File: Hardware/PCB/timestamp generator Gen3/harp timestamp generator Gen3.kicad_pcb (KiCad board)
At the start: 4 copper layers, 124.5 x 80.4 mm, 153 parts, among them IC1 MCP73831, IC10 SN74LVC1G125DBVT, IC11 LP5951MFX-3.3/NOPB, IC12 SI8621BC, IC13 SI8621BC, IC14 SI8621BC, IC15 SI8621BC, IC16 SI8621BC, IC17 SI8621BC, IC18 SN74LVC1G125DBVT, IC19 SN74LVC1G125DBVT, IC2 USBLC6-2SC6, IC3 FT232RL-REEL, IC4 TPS2114, IC5 LP5951MFX-3.3/NOPB, IC6 ATXMEGA16A4U-A, IC7 M74VHC1GT126DF1G, IC8 M74VHC1GT126DF1G, IC9 M74VHC1GT126DF1G, Q1 RTU002P02T106, Q2 BC817-40W, Q3 SBC817, Q4 DMG1012UW, Q5 DMP2035U-7, T1 BC850, T10 BC850, T2 BC850, T3 BC850, T4 BC850, T5 BC850, T6 BC850, T7 BC850, T8 BC850, T9 BC850, X1 B2B-XH-A(LF)(SN)

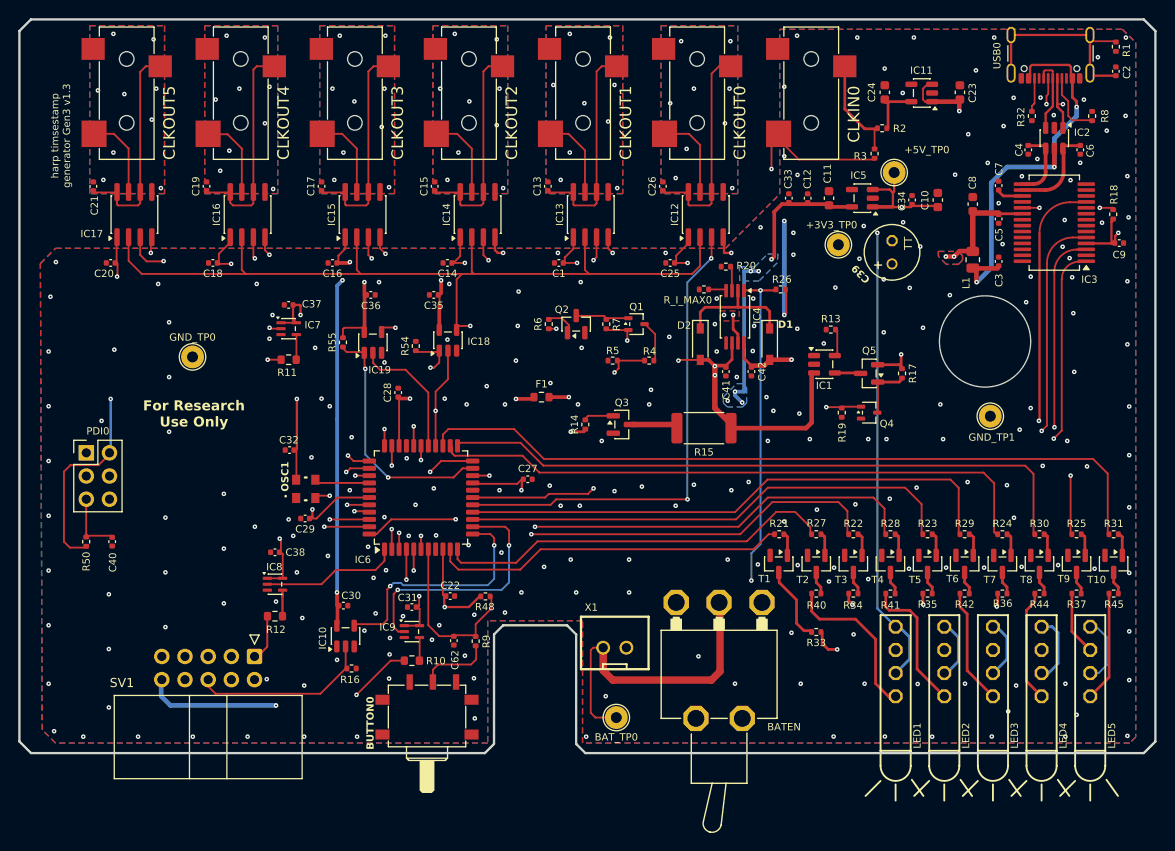
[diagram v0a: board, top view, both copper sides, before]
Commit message: Fix Q2 footprint and button's GND pin.
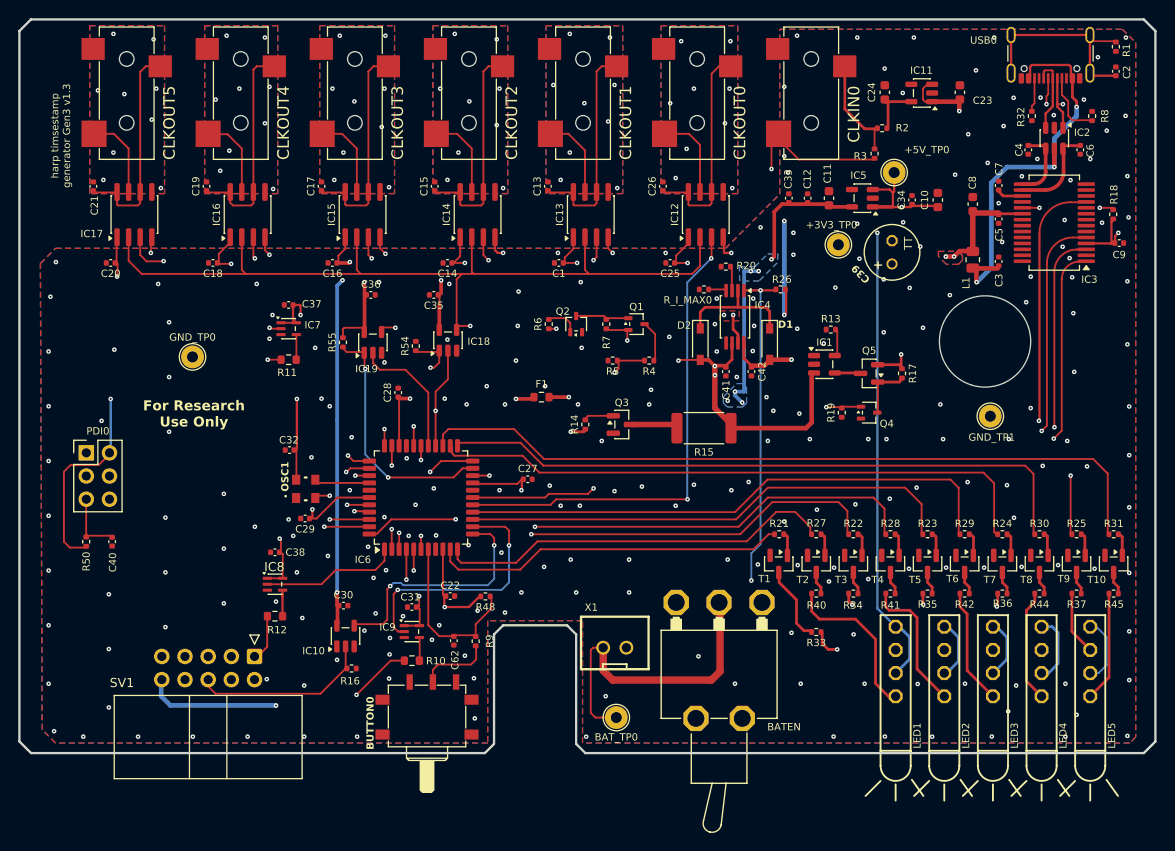
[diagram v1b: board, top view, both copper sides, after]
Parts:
- Q2: footprint Package_TO_SOT_SMD:SOT-23 -> Package_TO_SOT_SMD:SOT-323_SC-70
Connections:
- BUTTON0 pad 1: unconnected-(BUTTON0-A-Pad1) -> GND
- BUTTON0 pad 3: GND -> unconnected-(BUTTON0-C-Pad3)
